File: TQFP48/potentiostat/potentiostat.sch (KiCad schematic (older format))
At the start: 5 parts, among them U1 AD5941BCPZ

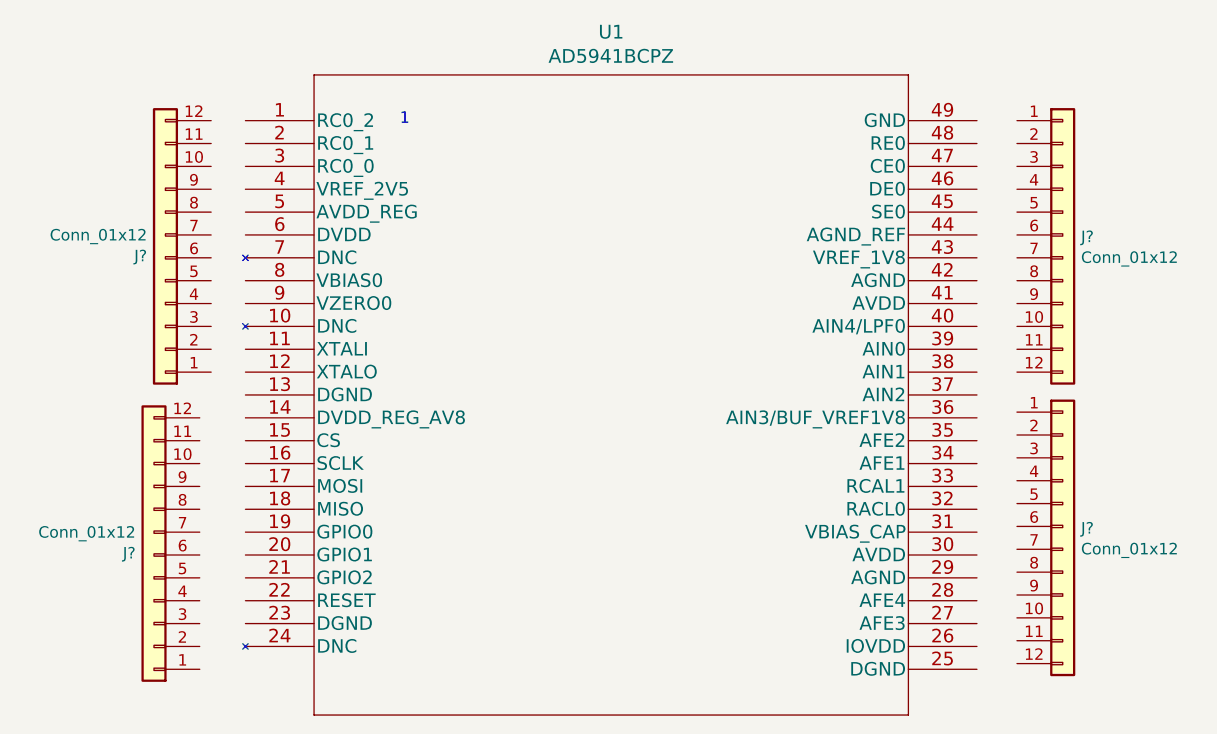
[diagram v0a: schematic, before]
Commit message: add better connections(3 12pin 1 13 pin generic pin headers)
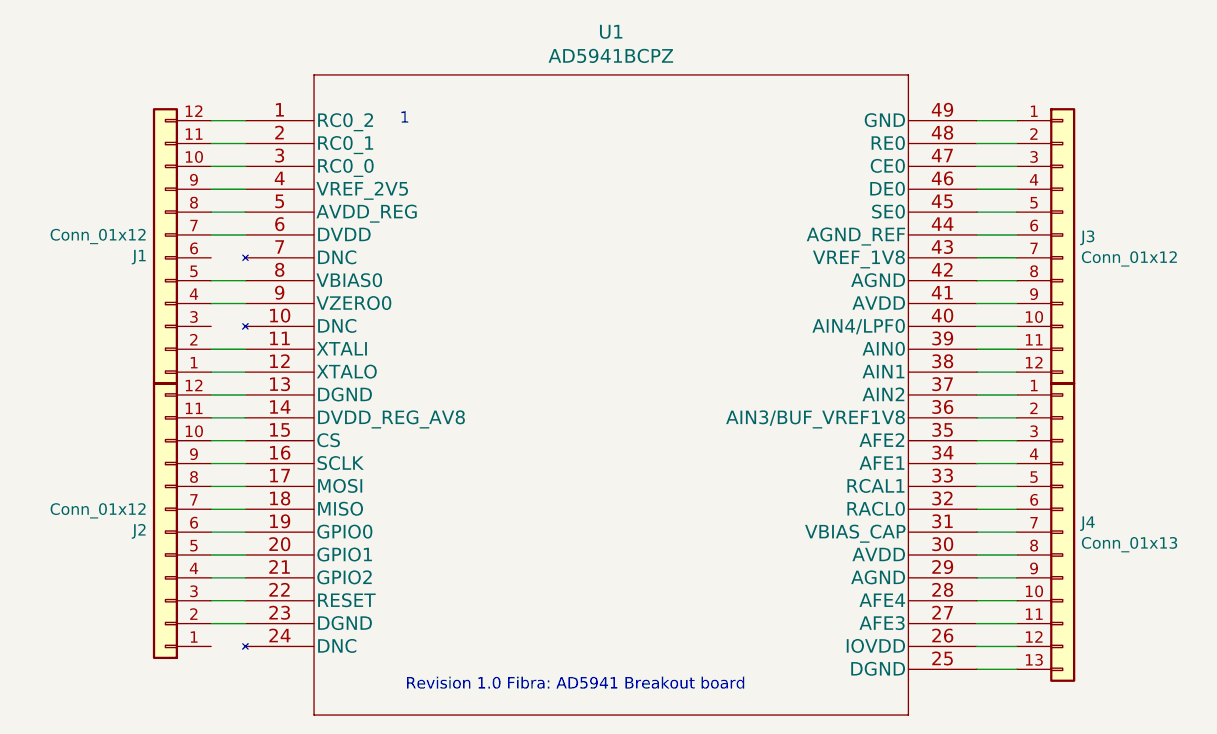
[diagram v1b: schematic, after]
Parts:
- removed J?: Conn_01x12, symbol Connector_Generic:Conn_01x12
- added J4: Conn_01x13, Connector_PinHeader_1.00mm:PinHeader_1x13_P1.00mm_Vertical, symbol Connector_Generic:Conn_01x13
- J1, J2, J3: renamed from J?; footprint (none) -> Connector_PinHeader_1.00mm:PinHeader_1x12_P1.00mm_Vertical
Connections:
- net at U1.1 (RC0_2): now also J1.12 (Pin_12)
- net at U1.11 (XTALI): now also J1.2 (Pin_2)
- net at U1.12 (XTALO): now also J1.1 (Pin_1)
- net at U1.13 (DGND): now also J2.12 (Pin_12)
- net at U1.14 (DVDD_REG_AV8): now also J2.11 (Pin_11)
- net at U1.15 (CS): now also J2.10 (Pin_10)
- net at U1.16 (SCLK): now also J2.9 (Pin_9)
- net at U1.17 (MOSI): now also J2.8 (Pin_8)
- net at U1.18 (MISO): now also J2.7 (Pin_7)
- net at U1.19 (GPIO0): now also J2.6 (Pin_6)
- net at U1.2 (RC0_1): now also J1.11 (Pin_11)
- net at U1.20 (GPIO1): now also J2.5 (Pin_5)
- net at U1.21 (GPIO2): now also J2.4 (Pin_4)
- net at U1.22 (RESET): now also J2.3 (Pin_3)
- net at U1.23 (DGND): now also J2.2 (Pin_2)
- net at U1.25 (DGND): now also J4.13 (Pin_13)
- net at U1.26 (IOVDD): now also J4.12 (Pin_12)
- net at U1.27 (AFE3): now also J4.11 (Pin_11)
- net at U1.28 (AFE4): now also J4.10 (Pin_10)
- net at U1.29 (AGND): now also J4.9 (Pin_9)
- net at U1.3 (RC0_0): now also J1.10 (Pin_10)
- net at U1.30 (AVDD): now also J4.8 (Pin_8)
- net at U1.31 (VBIAS_CAP): now also J4.7 (Pin_7)
- net at U1.32 (RACL0): now also J4.6 (Pin_6)
- net at U1.33 (RCAL1): now also J4.5 (Pin_5)
- net at U1.34 (AFE1): now also J4.4 (Pin_4)
- net at U1.35 (AFE2): now also J4.3 (Pin_3)
- net at U1.36 (AIN3/BUF_VREF1V8): now also J4.2 (Pin_2)
- net at U1.37 (AIN2): now also J4.1 (Pin_1)
- net at U1.38 (AIN1): now also J3.12 (Pin_12)
- net at U1.39 (AIN0): now also J3.11 (Pin_11)
- net at U1.4 (VREF_2V5): now also J1.9 (Pin_9)
- net at U1.40 (AIN4/LPF0): now also J3.10 (Pin_10)
- net at U1.41 (AVDD): now also J3.9 (Pin_9)
- net at U1.42 (AGND): now also J3.8 (Pin_8)
- net at U1.43 (VREF_1V8): now also J3.7 (Pin_7)
- net at U1.44 (AGND_REF): now also J3.6 (Pin_6)
- net at U1.45 (SE0): now also J3.5 (Pin_5)
- net at U1.46 (DE0): now also J3.4 (Pin_4)
- net at U1.47 (CE0): now also J3.3 (Pin_3)
- net at U1.48 (RE0): now also J3.2 (Pin_2)
- net at U1.49 (GND): now also J3.1 (Pin_1)
- net at U1.5 (AVDD_REG): now also J1.8 (Pin_8)
- net at U1.6 (DVDD): now also J1.7 (Pin_7)
- net at U1.8 (VBIAS0): now also J1.5 (Pin_5)
- net at U1.9 (VZERO0): now also J1.4 (Pin_4)
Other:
- note added: "Revision 1.0 Fibra: AD5941 Breakout board"
- moved on the sheet: J2
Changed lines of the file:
@@
 $EndComp
 $Comp
-L Connector_Generic:Conn_01x12 J?
+L Connector_Generic:Conn_01x12 J3
 U 1 1 6391DBC0
 P 7575 2750
-F 0 "J?" H 7655 2742 50  0000 L CNN
+F 0 "J3" H 7655 2742 50  0000 L CNN
 F 1 "Conn_01x12" H 7655 2651 50  0000 L CNN
-F 2 "" H 7575 2750 50  0001 C CNN
+F 2 "Connector_PinHeader_1.00mm:PinHeader_1x12_P1.00mm_Vertical" H 7575 2750 50  0001 C CNN
 F 3 "~" H 7575 2750 50  0001 C CNN
 	1    7575 2750
@@
 $EndComp
 $Comp
-L Connector_Generic:Conn_01x12 J?
-U 1 1 6391F2DC
-P 7575 4025
-F 0 "J?" H 7655 4017 50  0000 L CNN
-F 1 "Conn_01x12" H 7655 3926 50  0000 L CNN
-F 2 "" H 7575 4025 50  0001 C CNN
-F 3 "~" H 7575 4025 50  0001 C CNN
-	1    7575 4025
-	1    0    0    -1
-$EndComp
-$Comp
-L Connector_Generic:Conn_01x12 J?
+L Connector_Generic:Conn_01x12 J1
 U 1 1 6391FF4F
 P 3650 2850
-F 0 "J?" H 3730 2842 50  0000 L CNN
+F 0 "J1" H 3730 2842 50  0000 L CNN
 F 1 "Conn_01x12" H 3730 2751 50  0000 L CNN
-F 2 "" H 3650 2850 50  0001 C CNN
+F 2 "Connector_PinHeader_1.00mm:PinHeader_1x12_P1.00mm_Vertical" H 3650 2850 50  0001 C CNN
 F 3 "~" H 3650 2850 50  0001 C CNN
 	1    3650 2850
@@
 $EndComp
 $Comp
-L Connector_Generic:Conn_01x12 J?
+L Connector_Generic:Conn_01x12 J2
 U 1 1 6392088E
-P 3600 4150
-F 0 "J?" H 3680 4142 50  0000 L CNN
-F 1 "Conn_01x12" H 3680 4051 50  0000 L CNN
-F 2 "" H 3600 4150 50  0001 C CNN
-F 3 "~" H 3600 4150 50  0001 C CNN
-	1    3600 4150
+P 3650 4050
+F 0 "J2" H 3730 4042 50  0000 L CNN
+F 1 "Conn_01x12" H 3730 3951 50  0000 L CNN
+F 2 "Connector_PinHeader_1.00mm:PinHeader_1x12_P1.00mm_Vertical" H 3650 4050 50  0001 C CNN
+F 3 "~" H 3650 4050 50  0001 C CNN
+	1    3650 4050
 	-1   0    0    1
 $EndComp
+Wire Wire Line
+	4000 2250 3850 2250
+Wire Wire Line
+	3850 2350 4000 2350
+Wire Wire Line
+	3850 2450 4000 2450
+Wire Wire Line
+	3850 2550 4000 2550
+Wire Wire Line
+	4000 2650 3850 2650
+Wire Wire Line
+	3850 2750 4000 2750
+Wire Wire Line
+	3850 2950 4000 2950
+Wire Wire Line
+	3850 3050 4000 3050
+Wire Wire Line
+	3850 3250 4000 3250
+Wire Wire Line
+	3850 3350 4000 3350
+Wire Wire Line
+	4000 3450 3850 3450
+Wire Wire Line
+	3850 3550 4000 3550
+Wire Wire Line
+	4000 3650 3850 3650
+Wire Wire Line
+	3850 3750 4000 3750
+Wire Wire Line
+	3850 3850 4000 3850
+Wire Wire Line
+	3850 3950 4000 3950
+Wire Wire Line
+	3850 4050 4000 4050
+Wire Wire Line
+	3850 4150 4000 4150
+Wire Wire Line
+	3850 4250 4000 4250
+Wire Wire Line
+	3850 4350 4000 4350
+Wire Wire Line
+	4000 4450 3850 4450
+Wire Wire Line
+	7375 2250 7200 2250
+Wire Wire Line
+	7200 2350 7375 2350
+Wire Wire Line
+	7200 2450 7375 2450
+Wire Wire Line
+	7200 2550 7375 2550
+Wire Wire Line
+	7200 2650 7375 2650
+Wire Wire Line
+	7200 2750 7375 2750
+Wire Wire Line
+	7200 2850 7375 2850
+Wire Wire Line
+	7200 2950 7375 2950
+Wire Wire Line
+	7200 3050 7375 3050
+Wire Wire Line
+	7375 3150 7200 3150
+Wire Wire Line
+	7200 3250 7375 3250
+Wire Wire Line
+	7200 3350 7375 3350
+$Comp
+L Connector_Generic:Conn_01x13 J4
+U 1 1 638BBA45
+P 7575 4050
+F 0 "J4" H 7655 4092 50  0000 L CNN
+F 1 "Conn_01x13" H 7655 4001 50  0000 L CNN
+F 2 "Connector_PinHeader_1.00mm:PinHeader_1x13_P1.00mm_Vertical" H 7575 4050 50  0001 C CNN
+F 3 "~" H 7575 4050 50  0001 C CNN
+	1    7575 4050
+	1    0    0    -1
+$EndComp
+Wire Wire Line
+	7200 3450 7375 3450
+Wire Wire Line
+	7200 3550 7375 3550
+Wire Wire Line
+	7200 3650 7375 3650
+Wire Wire Line
+	7200 3750 7375 3750
+Wire Wire Line
+	7200 3850 7375 3850
+Wire Wire Line
+	7200 3950 7375 3950
+Wire Wire Line
+	7200 4050 7375 4050
+Wire Wire Line
+	7200 4150 7375 4150
+Wire Wire Line
+	7200 4250 7375 4250
+Wire Wire Line
+	7200 4350 7375 4350
+Wire Wire Line
+	7200 4450 7375 4450
+Wire Wire Line
+	7200 4550 7375 4550
+Wire Wire Line
+	7200 4650 7375 4650
+Text Notes 4700 4750 0    50   ~ 0
+Revision 1.0 Fibra: AD5941 Breakout board
 $EndSCHEMATC
